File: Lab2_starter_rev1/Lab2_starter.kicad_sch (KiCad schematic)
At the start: 76 parts, among them J1 973582101, J10 Conn_01x02, J11 Conn_01x02, J12 Conn_01x02, J13 Conn_01x02, J14 Conn_01x02, J15 Conn_01x02, J16 Conn_01x02, J2 973582100, J3 973582101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

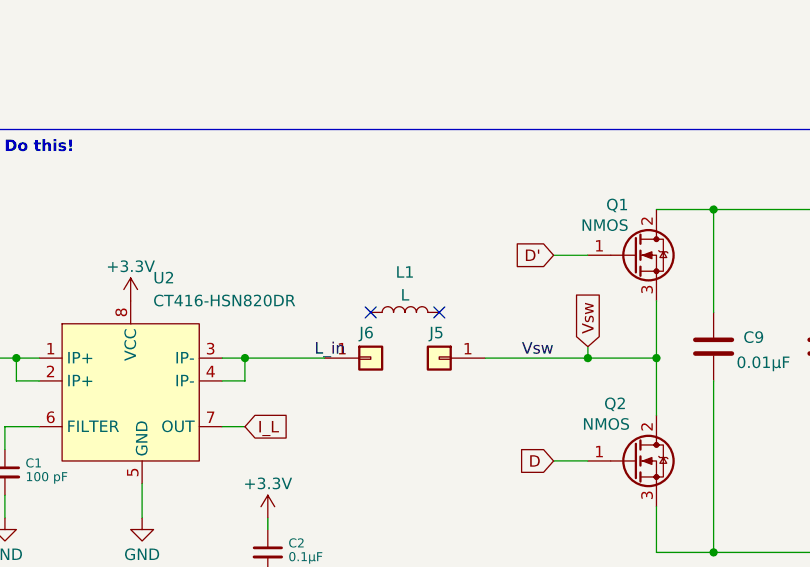
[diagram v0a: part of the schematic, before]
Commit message: Updated for first PCB upload
Added missing vias to some grounds
Increased width of a few wires
Moved many silkscreens
Added keepout zone for inductor
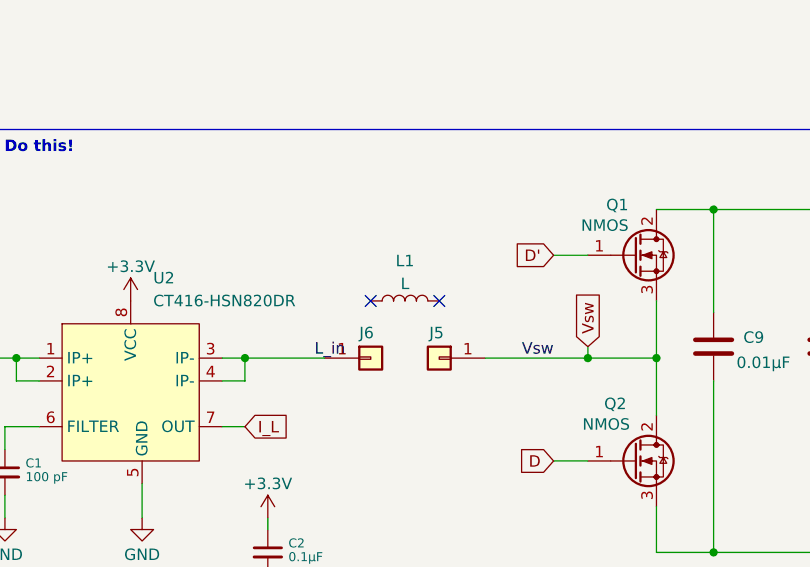
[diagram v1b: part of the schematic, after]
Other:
- moved on the sheet: L1
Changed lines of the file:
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@@
 	)
 	(no_connect
-		(at 95.25 36.83)
+		(at 95.25 35.56)
 	)
 	(no_connect
@@
 	)
 	(no_connect
-		(at 87.63 36.83)
+		(at 87.63 35.56)
 	)
 	(no_connect
@@
 	(symbol
 		(lib_id "Device:L")
-		(at 91.44 36.83 90)
+		(at 91.44 35.56 90)
 		(unit 1)
 		(exclude_from_sim no)
@@
 		(fields_autoplaced yes)
 		(property "Reference" "L1"
-			(at 91.44 32.385 90)
+			(at 91.44 31.115 90)
 			(effects
 				(font
@@
 		)
 		(property "Value" "L"
-			(at 91.44 34.925 90)
+			(at 91.44 33.655 90)
 			(effects
 				(font
@@
 		)
 		(property "Footprint" "ECE462L:Inductor"
-			(at 91.44 36.83 0)
+			(at 91.44 35.56 0)
 			(effects
 				(font
@@
 		)
 		(property "Datasheet" "~"
-			(at 91.44 36.83 0)
+			(at 91.44 35.56 0)
 			(effects
 				(font
@@
 		)
 		(property "Description" ""
-			(at 91.44 36.83 0)
+			(at 91.44 35.56 0)
 			(effects
 				(font
